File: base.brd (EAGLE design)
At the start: 100 x 80 mm, 1 part, among them U1 XC7K160TFBG484

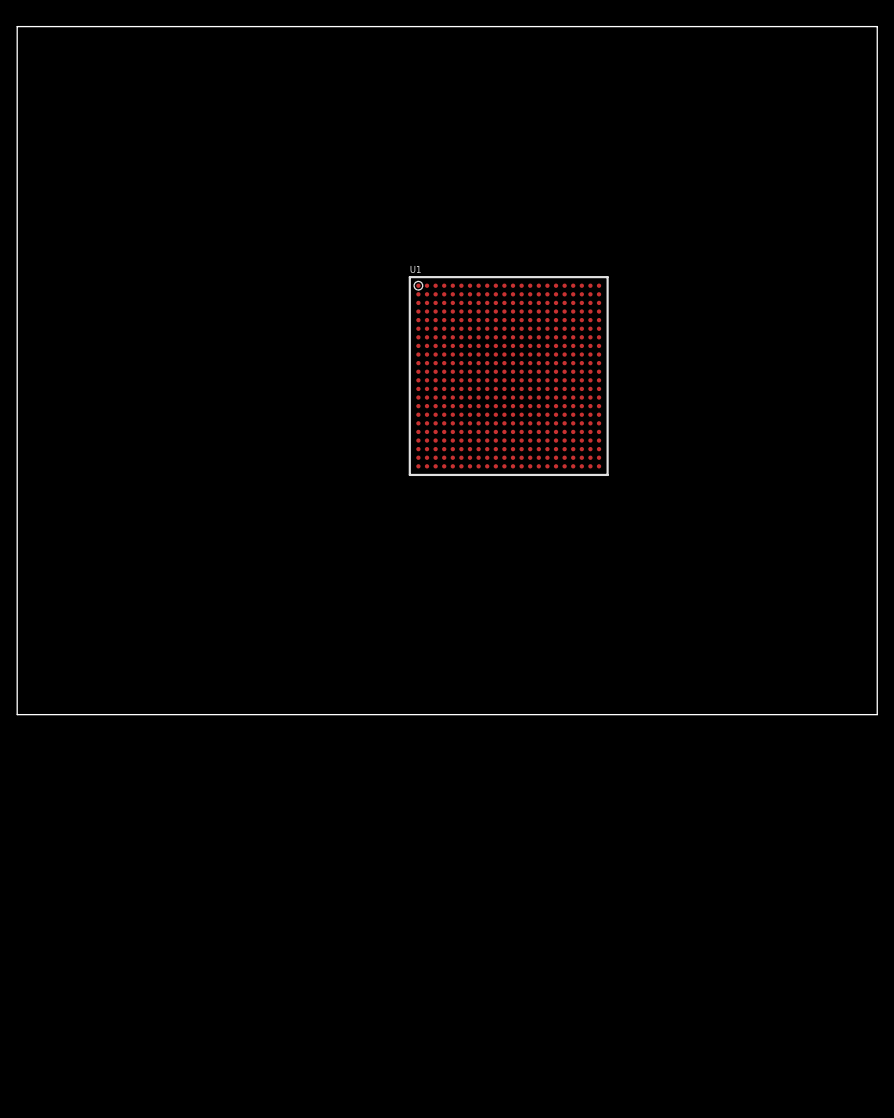
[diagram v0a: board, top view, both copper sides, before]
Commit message: adding DRAM.
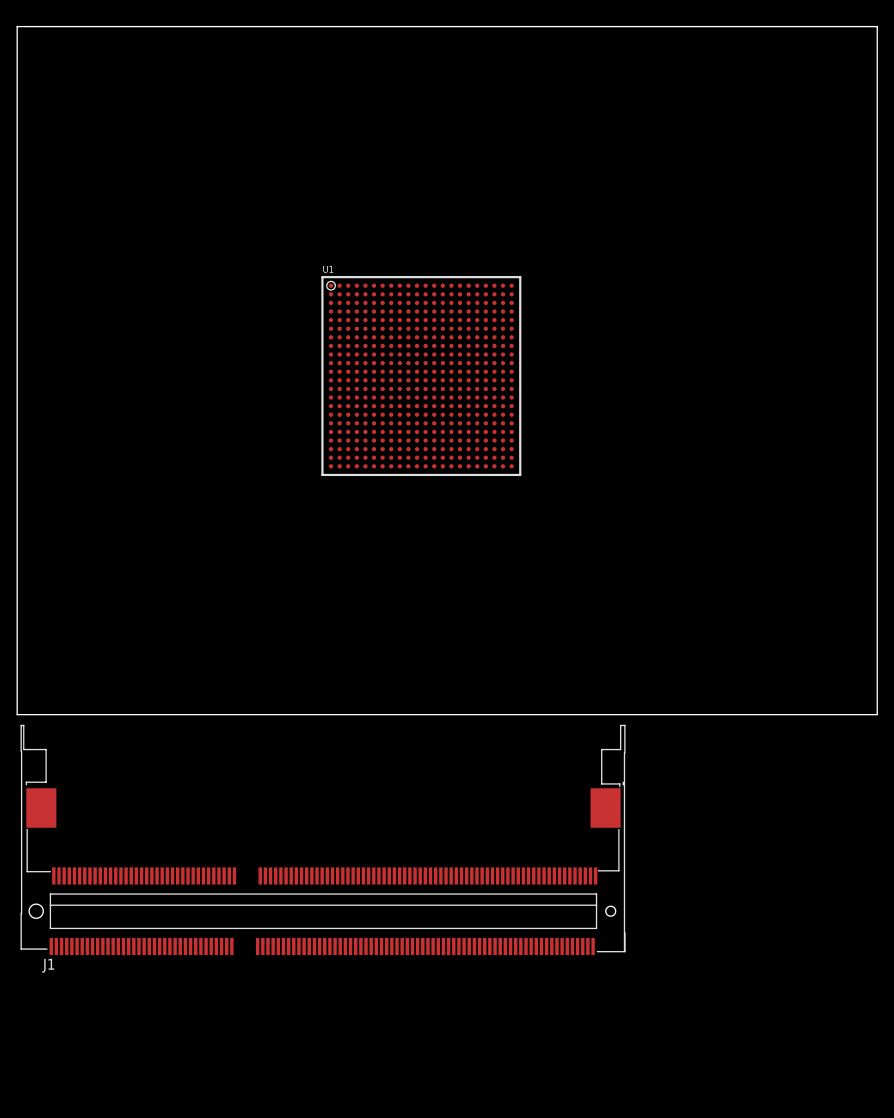
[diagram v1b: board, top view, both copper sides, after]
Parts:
- added J1: AS0A626-U2SN-7F, AS0A626-U2SN-7F:FOXCONN_AS0A626-U2SN-7F
- moved U1 10.2 mm to (47.0, 39.4)
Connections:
- removed net N$1: U1.AA17, U1.AB14, U1.T22, U1.U19, U1.V16, U1.Y20
- removed net N$2: U1.J7
- removed net N$3: U1.N7
- removed net N$4: U1.F22, U1.G19, U1.K20, U1.L17, U1.N21, U1.P18
- removed net N$5: U1.A17, U1.B14, U1.C21, U1.D18, U1.E15, U1.H16
- removed net N$6: U1.C11, U1.D8, U1.F12, U1.G9
- removed net N$7: U1.AA7, U1.T12, U1.U9, U1.V6, U1.W13, U1.Y10
- removed net N$8: U1.AB4, U1.M4, U1.N1, U1.R5, U1.T2, U1.W3
- new net VADJ_FPGA: U1.AA17, U1.AB14, U1.C11, U1.D8, U1.F12, U1.G9, U1.T22, U1.U19, U1.V16, U1.Y20
- new net VCC1V5_FPGA: U1.AA7, U1.AB4, U1.M4, U1.N1, U1.R5, U1.T12, U1.T2, U1.U9, U1.V6, U1.W13, U1.W3, U1.Y10
- net VCC2V5_FPGA: now also U1.A17, U1.B14, U1.C21, U1.D18, U1.E15, U1.F22, U1.G19, U1.H16, U1.J7, U1.K20, U1.L17, U1.N21, U1.N7, U1.P18

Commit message: dram wired.
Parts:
- moved J1 84.7 mm to (63.5, 57.1)
- moved U1 18.2 mm to (63.5, 31.8)
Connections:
- new net D_A0: J1.98, U1.W15
- new net D_A1: J1.97, U1.T15
- new net D_A10: J1.107, U1.F10
- new net D_A11: J1.84, U1.E11
- new net D_A12: J1.83, U1.D11
- new net D_A13: J1.119, U1.G11
- new net D_A14: J1.80, U1.G10
- new net D_A15: J1.78, U1.H12
- new net D_A2: J1.96, U1.U15
- new net D_A3: J1.95, U1.D10
- new net D_A4: J1.92, U1.C10
- new net D_A5: J1.91, U1.G13
- new net D_A6: J1.90, U1.F13
- new net D_A7: J1.86, U1.E13
- new net D_A8: J1.89, U1.E12
- new net D_A9: J1.85, U1.F11
- new net D_BA0: J1.109, U1.G12
- new net D_BA1: J1.108, U1.H9
- new net D_BA2: J1.79, U1.H8
- new net D_CAS_N: J1.115, U1.A10
- new net D_CKE0: J1.73, U1.G8
- new net D_CLK0_N: J1.103, U1.D9
- new net D_CLK0_P: J1.101, U1.B11
- new net D_CLK1_N: J1.104, U1.B10
- new net D_CLK1_P: J1.102, U1.C8
- new net D_D0: J1.5, U1.V18
- new net D_D1: J1.7, U1.U22
- new net D_D10: J1.33, U1.Y22
- new net D_D11: J1.35, U1.V20
- new net D_D12: J1.22, U1.AA19
- new net D_D13: J1.24, U1.AB21
- new net D_D14: J1.34, U1.W20
- new net D_D15: J1.36, U1.V10
- new net D_D16: J1.39, U1.AB15
- new net D_D17: J1.41, U1.AB16
- new net D_D18: J1.51, U1.W19
- new net D_D19: J1.53, U1.Y18
- new net D_D2: J1.15, U1.W22
- new net D_D20: J1.40, U1.Y17
- new net D_D21: J1.42, U1.AA16
- new net D_D22: J1.50, U1.Y19
- new net D_D23: J1.52, U1.W17
- new net D_D24: J1.57, U1.V15
- new net D_D25: J1.59, U1.AA14
- new net D_D26: J1.67, U1.W14
- new net D_D27: J1.69, U1.R16
- new net D_D28: J1.56, U1.AA15
- new net D_D29: J1.58, U1.U16
- new net D_D3: J1.17, U1.W21
- new net D_D30: J1.68, U1.T16
- new net D_D31: J1.70, U1.Y14
- new net D_D32: J1.129, U1.AA9
- new net D_D33: J1.131, U1.W11
- new net D_D34: J1.141, U1.Y6
- new net D_D35: J1.143, U1.R7
- new net D_D36: J1.130, U1.R6
- new net D_D37: J1.132, U1.AA10
- new net D_D38: J1.140, U1.AA8
- new net D_D39: J1.142, U1.W6
- new net D_D4: J1.4, U1.V22
- new net D_D40: J1.147, U1.Y7
- new net D_D41: J1.149, U1.W9
- new net D_D42: J1.157, U1.W7
- new net D_D43: J1.159, U1.Y8
- new net D_D44: J1.146, U1.U10
- new net D_D45: J1.148, U1.Y9
- new net D_D46: J1.158, U1.U6
- new net D_D47: J1.160, U1.V7
- new net D_D48: J1.163, U1.T9
- new net D_D49: J1.165, U1.W12
- new net D_D5: J1.6, U1.U17
- new net D_D50: J1.175, U1.U11
- new net D_D51: J1.177, U1.U12
- new net D_D52: J1.164, U1.AA11
- new net D_D53: J1.166, U1.T11
- new net D_D54: J1.174, U1.T8
- new net D_D55: J1.176, U1.T10
- new net D_D56: J1.181, U1.T13
- new net D_D57: J1.183, U1.U8
- new net D_D58: J1.191, U1.V13
- new net D_D59: J1.193, U1.V12
- new net D_D6: J1.16, U1.T20
- new net D_D60: J1.180, U1.AB13
- new net D_D61: J1.182, U1.AB12
- new net D_D62: J1.192, U1.U13
- new net D_D63: J1.194, U1.V8
- new net D_D7: J1.18, U1.T21
- new net D_D8: J1.21, U1.AA20
- new net D_D9: J1.23, U1.AB20
- new net D_DM0: J1.11, U1.U21
- new net D_DM1: J1.28, U1.Y21
- new net D_DM2: J1.46, U1.V19
- new net D_DM3: J1.63, U1.AB17
- new net D_DM4: J1.136, U1.AB10
- new net D_DM5: J1.153, U1.U7
- new net D_DM6: J1.170, U1.V9
- new net D_DM7: J1.187, U1.AB11
- new net D_DQS0_N: J1.10, U1.U18
- new net D_DQS0_P: J1.12, U1.T18
- new net D_DQS1_N: J1.27, U1.AB22
- new net D_DQS1_P: J1.29, U1.AA21
- new net D_DQS2_N: J1.45, U1.AB18
- new net D_DQS2_P: J1.47, U1.AA18
- new net D_DQS3_N: J1.62, U1.Y16
- new net D_DQS3_P: J1.64, U1.W16
- new net D_DQS4_N: J1.135, U1.H13
- new net D_DQS4_P: J1.137, U1.H14
- new net D_DQS5_N: J1.152, U1.E9
- new net D_DQS5_P: J1.154, U1.F9
- new net D_DQS6_N: J1.169, U1.A8
- new net D_DQS6_P: J1.171, U1.A9
- new net D_DQS7_N: J1.186, U1.AA6
- new net D_DQS7_P: J1.188, U1.AB6
- new net D_NC: J1.120, J1.121, J1.122, J1.125, J1.74, J1.77
- new net D_ODT0: J1.116, U1.AB8
- new net D_RAS_N: J1.110, U1.A11
- new net D_RESET_N: J1.30, U1.W10
- new net D_S0_N: J1.114, U1.AA5
- new net D_SCL: J1.202
- new net D_SDA: J1.200
- new net D_VSS: J1.127, J1.128, J1.13, J1.133, J1.134, J1.138, J1.139, J1.14, J1.144, J1.145, J1.150, J1.151, J1.155, J1.156, J1.161, J1.162, J1.167, J1.168, J1.172, J1.173, J1.178, J1.179, J1.184, J1.185, J1.189, J1.19, J1.190, J1.195, J1.196, J1.2, J1.20, J1.25, J1.26, J1.3, J1.31, J1.32, J1.37, J1.38, J1.43, J1.44, J1.48, J1.49, J1.54, J1.55, J1.60, J1.61, J1.65, J1.66, J1.71, J1.72, J1.8, J1.9
- new net D_WE_N: J1.113, U1.B8
- new net VCC3V3: J1.199
- new net VTTDDR: J1.203, J1.204
- new net VTTVREF: J1.1, J1.124, J1.126, U1.C20, U1.C9, U1.D14, U1.F14, U1.K17, U1.L4, U1.R19, U1.U20, U1.V17, U1.Y11, U1.Y12, U1.Y4
- net GND: now also J1.197, J1.198, J1.201
- net VCC1V5_FPGA: now also J1.100, J1.105, J1.106, J1.111, J1.112, J1.117, J1.118, J1.123, J1.75, J1.76, J1.81, J1.82, J1.87, J1.88, J1.93, J1.94, J1.99

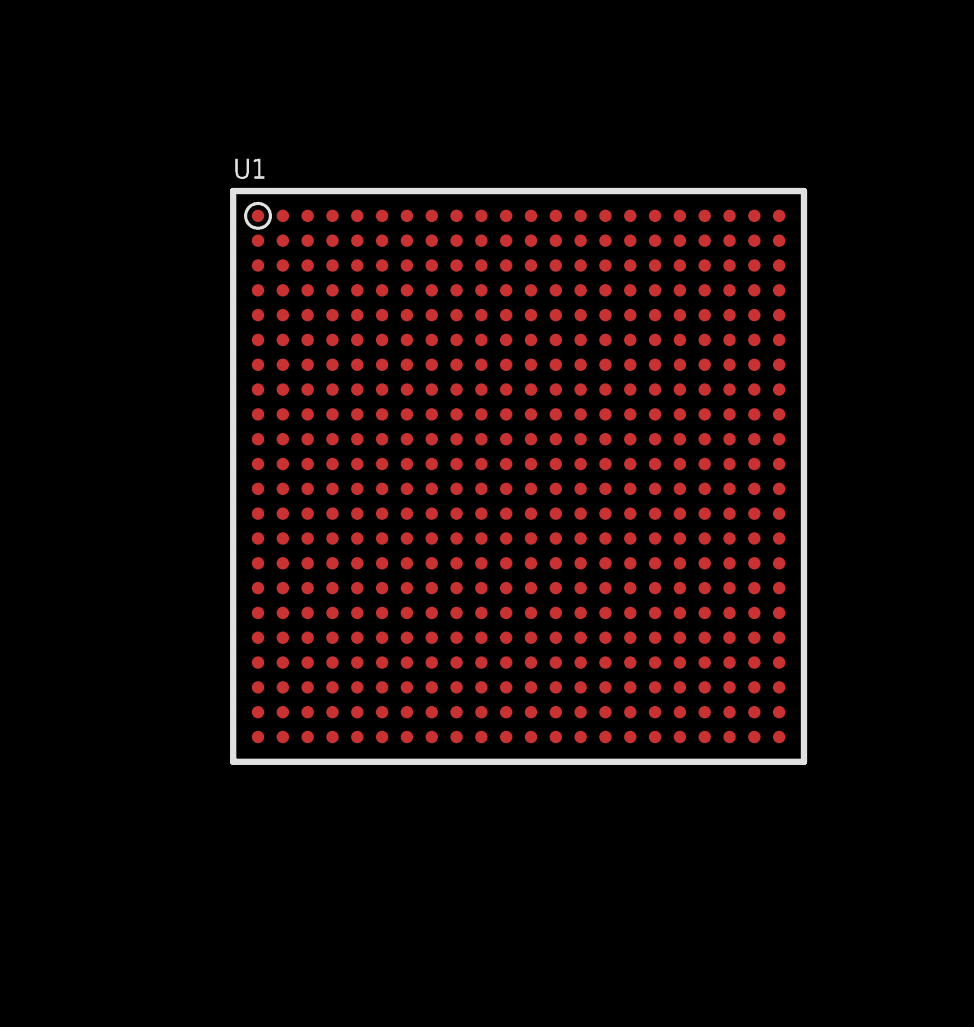
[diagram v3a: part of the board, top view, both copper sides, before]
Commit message: reverting dram, bigger chip.
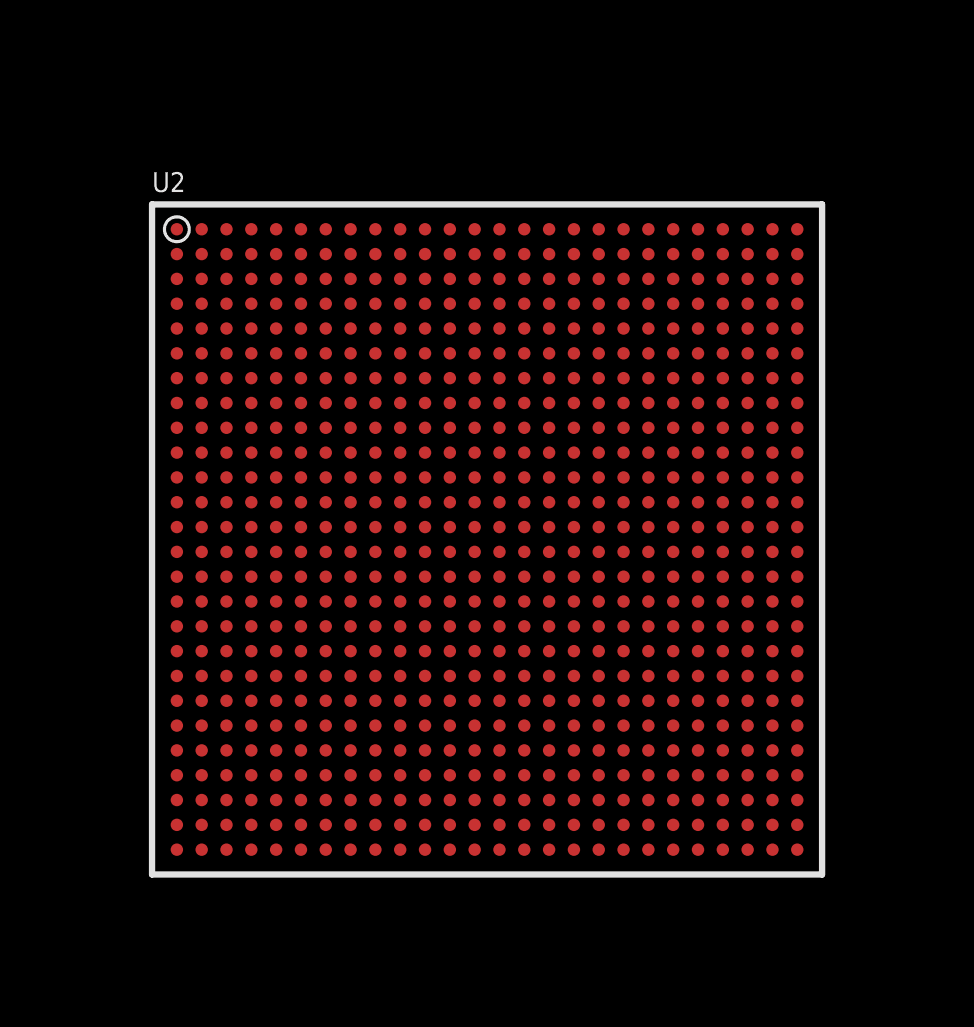
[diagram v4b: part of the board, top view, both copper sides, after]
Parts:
- removed U1: XC7K160TFBG484, xilinx_devices_V6:FF484
- added U2: XC7K160TFBG676, xilinx_devices_V6:FF676
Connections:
- removed net FPGA_CCLK: U1.G7
- removed net FPGA_DONE: U1.P6
- removed net FPGA_INIT_B: U1.L7
- removed net FPGA_M0: U1.H7
- removed net FPGA_M1: U1.H6
- removed net FPGA_M2: U1.J5
- removed net FPGA_PROG_B: U1.M6
- removed net FPGA_TCK_BUF: U1.K7
- removed net FPGA_TDI_BUF: U1.K6
- removed net FPGA_TMS_BUF: U1.L6
- removed net FPGA_VBATT: U1.P7
- removed net JTAG_TDO: U1.J6
- removed net MGTAVCC: U1.A6, U1.C6, U1.E6, U1.G6
- removed net MGTAVTT: U1.A2, U1.C2, U1.E2, U1.G2
- removed net MGTVCCAUX: U1.J4
- removed net VADJ_FPGA: U1.AA17, U1.AB14, U1.C11, U1.D8, U1.F12, U1.G9, U1.T22, U1.U19, U1.V16, U1.Y20
- removed net VCC2V5_FPGA: U1.A17, U1.B14, U1.C21, U1.D18, U1.E15, U1.F22, U1.G19, U1.H16, U1.J7, U1.K20, U1.L17, U1.M7, U1.N21, U1.N7, U1.P18
- removed net VCCINT_FPGA: U1.J11, U1.J13, U1.J15, U1.J9, U1.K14, U1.K8, U1.L15, U1.L9, U1.M14, U1.M8, U1.N15, U1.N9, U1.P14, U1.R15
- removed net VCC_AUX: U1.K10, U1.M10, U1.P10, U1.P12, U1.P8, U1.R11, U1.R9
- removed net VCC_BRAM: U1.L13, U1.N13, U1.R13
- removed net XADC_AGND: U1.K11, U1.L11
- removed net XADC_DXN: U1.N11
- removed net XADC_DXP: U1.N12
- removed net XADC_VCC: U1.K12
- removed net XADC_VN_R: U1.M11
- removed net XADC_VP_R: U1.L12
- removed net XADC_VREFP: U1.M12
- new net F_CCLK: U2.C8
- new net F_DONE: U2.J7
- new net F_INIT_N: U2.G7
- new net F_M0: U2.T5
- new net F_M1: U2.T2
- new net F_M2: U2.P5
- new net F_PROG_N: U2.P6
- new net F_TCK_BUF: U2.L8
- new net F_TDI_BUF: U2.R6
- new net F_TDO: U2.R7
- new net F_TMS_BUF: U2.N8
- new net F_VBATT: U2.E8
- new net VADJ_F: U2.A11, U2.AA21, U2.AC25, U2.AD22, U2.AF26, U2.B8, U2.C15, U2.D12, U2.E9, U2.G13, U2.H10, U2.K24, U2.N25, U2.P22, U2.R19, U2.T16, U2.T26, U2.U23, U2.V20, U2.Y24
- new net VCC1V5_F: U2.AA1, U2.AA11, U2.AB18, U2.AB8, U2.AC15, U2.AC5, U2.AD12, U2.AD2, U2.AE19, U2.AE9, U2.AF16, U2.AF6, U2.U3, U2.V10, U2.W17, U2.W7, U2.Y14, U2.Y4
- new net VCC2V5_F: U2.A21, U2.B18, U2.C25, U2.D22, U2.E19, U2.F16, U2.F26, U2.G23, U2.H20, U2.J17, U2.L21, U2.L7, U2.M18, U2.P7, U2.T6
- net D_A0: no longer U1.W15
- net D_A1: no longer U1.T15
- net D_A10: no longer U1.F10
- net D_A11: no longer U1.E11
- net D_A12: no longer U1.D11
- net D_A13: no longer U1.G11
- net D_A14: no longer U1.G10
- net D_A15: no longer U1.H12
- net D_A2: no longer U1.U15
- net D_A3: no longer U1.D10
- net D_A4: no longer U1.C10
- net D_A5: no longer U1.G13
- net D_A6: no longer U1.F13
- net D_A7: no longer U1.E13
- net D_A8: no longer U1.E12
- net D_A9: no longer U1.F11
- net D_BA0: no longer U1.G12
- net D_BA1: no longer U1.H9
- net D_BA2: no longer U1.H8
- net D_CAS_N: no longer U1.A10
- net D_CKE0: no longer U1.G8
- net D_CLK0_N: no longer U1.D9
- net D_CLK0_P: no longer U1.B11
- net D_CLK1_N: no longer U1.B10
- net D_CLK1_P: no longer U1.C8
- net D_D0: no longer U1.V18
- net D_D1: no longer U1.U22
- net D_D10: no longer U1.Y22
- net D_D11: no longer U1.V20
- net D_D12: no longer U1.AA19
- net D_D13: no longer U1.AB21
- net D_D14: no longer U1.W20
- net D_D15: no longer U1.V10
- net D_D16: no longer U1.AB15
- net D_D17: no longer U1.AB16
- net D_D18: no longer U1.W19
- net D_D19: no longer U1.Y18
- net D_D2: no longer U1.W22
- net D_D20: no longer U1.Y17
- net D_D21: no longer U1.AA16
- net D_D22: no longer U1.Y19
- net D_D23: no longer U1.W17
- net D_D24: no longer U1.V15
- net D_D25: no longer U1.AA14
- net D_D26: no longer U1.W14
- net D_D27: no longer U1.R16
- net D_D28: no longer U1.AA15
- net D_D29: no longer U1.U16
- net D_D3: no longer U1.W21
- net D_D30: no longer U1.T16
- net D_D31: no longer U1.Y14
- net D_D32: no longer U1.AA9
- net D_D33: no longer U1.W11
- net D_D34: no longer U1.Y6
- net D_D35: no longer U1.R7
- net D_D36: no longer U1.R6
- net D_D37: no longer U1.AA10
- net D_D38: no longer U1.AA8
- net D_D39: no longer U1.W6
- net D_D4: no longer U1.V22
- net D_D40: no longer U1.Y7
- net D_D41: no longer U1.W9
- net D_D42: no longer U1.W7
- net D_D43: no longer U1.Y8
- net D_D44: no longer U1.U10
- net D_D45: no longer U1.Y9
- net D_D46: no longer U1.U6
- net D_D47: no longer U1.V7
- net D_D48: no longer U1.T9
- net D_D49: no longer U1.W12
- net D_D5: no longer U1.U17
- net D_D50: no longer U1.U11
- net D_D51: no longer U1.U12
- net D_D52: no longer U1.AA11
- net D_D53: no longer U1.T11
- net D_D54: no longer U1.T8
- net D_D55: no longer U1.T10
- net D_D56: no longer U1.T13
- net D_D57: no longer U1.U8
- net D_D58: no longer U1.V13
- net D_D59: no longer U1.V12
- net D_D6: no longer U1.T20
- net D_D60: no longer U1.AB13
- net D_D61: no longer U1.AB12
- net D_D62: no longer U1.U13
- net D_D63: no longer U1.V8
- net D_D7: no longer U1.T21
- net D_D8: no longer U1.AA20
- net D_D9: no longer U1.AB20
- net D_DM0: no longer U1.U21
- net D_DM1: no longer U1.Y21
- net D_DM2: no longer U1.V19
- net D_DM3: no longer U1.AB17
- net D_DM4: no longer U1.AB10
- net D_DM5: no longer U1.U7
- net D_DM6: no longer U1.V9
- net D_DM7: no longer U1.AB11
- net D_DQS0_N: no longer U1.U18
- net D_DQS0_P: no longer U1.T18
- net D_DQS1_N: no longer U1.AB22
- net D_DQS1_P: no longer U1.AA21
- net D_DQS2_N: no longer U1.AB18
- net D_DQS2_P: no longer U1.AA18
- net D_DQS3_N: no longer U1.Y16
- net D_DQS3_P: no longer U1.W16
- net D_DQS4_N: no longer U1.H13
- net D_DQS4_P: no longer U1.H14
- net D_DQS5_N: no longer U1.E9
- net D_DQS5_P: no longer U1.F9
- net D_DQS6_N: no longer U1.A8
- net D_DQS6_P: no longer U1.A9
- net D_DQS7_N: no longer U1.AA6
- net D_DQS7_P: no longer U1.AB6
- net D_ODT0: no longer U1.AB8
- net D_RAS_N: no longer U1.A11
- net D_RESET_N: no longer U1.W10
- net D_S0_N: no longer U1.AA5
- net D_WE_N: no longer U1.B8
- net GND: now also U2.A1, U2.A16, U2.A2, U2.A26, U2.A5, U2.A6, U2.A7, U2.AA16, U2.AA26, U2.AA6, U2.AB13, U2.AB23, U2.AB3, U2.AC10, U2.AC20, U2.AD17, U2.AD7, U2.AE14, U2.AE24, U2.AE4, U2.AF1, U2.AF11, U2.AF21, U2.B13, U2.B23, U2.B4, U2.B7, U2.C1, U2.C10, U2.C20, U2.C5, U2.C7, U2.D17, U2.D4, U2.D7, U2.E1, U2.E14, U2.E2, U2.E24, U2.E5, U2.E7, U2.F11, U2.F21, U2.F3, U2.F4, U2.F7, U2.G1, U2.G18, U2.G5, U2.G8, U2.H15, U2.H25, U2.H4, U2.H7, U2.J1, U2.J12, U2.J2, U2.J22, U2.J5, U2.K11, U2.K13, U2.K19, U2.K3, U2.K4, U2.K7, U2.K9, U2.L1, U2.L10, U2.L12, U2.L14, U2.L16, U2.L26, U2.L5, U2.M13, U2.M15, U2.M23, U2.M4, U2.M7, U2.M9, U2.N1, U2.N10, U2.N14, U2.N2, U2.N20, U2.N5, U2.N7, U2.P13, U2.P15, U2.P17, U2.P3, U2.P4, U2.P9, U2.R1, U2.R10, U2.R14, U2.R2, U2.R24, U2.R5, U2.R8, U2.T1, U2.T11, U2.T13, U2.T15, U2.T21, U2.T3, U2.T4, U2.T9, U2.U10, U2.U12, U2.U14, U2.U18, U2.U8, U2.V15, U2.V25, U2.V5, U2.W12, U2.W2, U2.W22, U2.Y19, U2.Y9; no longer U1.A1, U1.A12, U1.A22, U1.A5, U1.A7, U1.AA12, U1.AA2, U1.AA22, U1.AB19, U1.AB9, U1.B19, U1.B3, U1.B4, U1.B7, U1.B9, U1.C1, U1.C16, U1.C5, U1.C7, U1.D13, U1.D3, U1.D4, U1.D7, U1.E1, U1.E10, U1.E20, U1.E5, U1.E7, U1.F17, U1.F3, U1.F4, U1.F7, U1.G1, U1.G14, U1.G5, U1.H11, U1.H21, U1.H3, U1.H4, U1.H5, U1.J1, U1.J10, U1.J12, U1.J14, U1.J18, U1.J2, U1.J3, U1.J8, U1.K13, U1.K15, U1.K5, U1.K9, U1.L10, U1.L14, U1.L2, U1.L22, U1.L8, U1.M13, U1.M15, U1.M19, U1.M9, U1.N10, U1.N14, U1.N16, U1.N6, U1.N8, U1.P11, U1.P13, U1.P15, U1.P3, U1.P9, U1.R10, U1.R12, U1.R14, U1.R20, U1.R8, U1.T17, U1.T7, U1.U14, U1.U4, U1.V1, U1.V11, U1.V21, U1.W18, U1.W8, U1.Y15, U1.Y5
- net VCC1V5_FPGA: no longer U1.AA7, U1.AB4, U1.M4, U1.N1, U1.R5, U1.T12, U1.T2, U1.U9, U1.V6, U1.W13, U1.W3, U1.Y10
- net VTTVREF: no longer U1.C20, U1.C9, U1.D14, U1.F14, U1.K17, U1.L4, U1.R19, U1.U20, U1.V17, U1.Y11, U1.Y12, U1.Y4

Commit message: updating for new lib.
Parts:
- added U$1: PCIEX4_SMALL_CARD, con-pcie-x4 short card:PCIEX4_SMALL_CARD
- moved U2 18.2 mm to (80.0, 33.0)
- moved J1 16.5 mm to (63.5, 73.7), turned to 180 degrees
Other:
- board size 100 x 80 mm -> 34 x 5.6 mm
